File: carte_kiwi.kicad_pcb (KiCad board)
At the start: 2 copper layers, 50 x 50 mm, 236 parts, among them IC1 MCP2562, P1 CONN_01X05, P2 CONN_01X03, P3 CONN_01X05, P4 CONN_01X03, P5 Serial Wire, P6 CAN_conn, P7 CONN_01X03, P8 CONN_01X03, P9 CAN_conn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

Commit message: ajout nom, url et export gerber
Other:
- board text added: "Phoenix Robotik Carte Kiwi"
- board text added: "https://github.com/PhoenixRobotik/kiwi-elec"
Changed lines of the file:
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@@
     (area 124.924999 84.924999 175.075001 135.075001)
     (thickness 1.6)
-    (drawings 18)
+    (drawings 20)
     (tracks 463)
     (zones 0)
@@
   (page A4)
   (layers
-    (0 F.Cu signal)
-    (31 B.Cu signal)
-    (32 B.Adhes user)
-    (33 F.Adhes user)
-    (34 B.Paste user)
-    (35 F.Paste user)
+    (0 F.Cu signal hide)
+    (31 B.Cu signal hide)
+    (32 B.Adhes user hide)
+    (33 F.Adhes user hide)
+    (34 B.Paste user hide)
+    (35 F.Paste user hide)
     (36 B.SilkS user)
     (37 F.SilkS user)
     (38 B.Mask user hide)
     (39 F.Mask user hide)
-    (40 Dwgs.User user)
-    (41 Cmts.User user)
-    (42 Eco1.User user)
-    (43 Eco2.User user)
+    (40 Dwgs.User user hide)
+    (41 Cmts.User user hide)
+    (42 Eco1.User user hide)
+    (43 Eco2.User user hide)
     (44 Edge.Cuts user)
-    (45 Margin user)
+    (45 Margin user hide)
     (46 B.CrtYd user)
     (47 F.CrtYd user)
@@
     (visible_elements FFFFFF7F)
     (pcbplotparams
-      (layerselection 0x00030_80000001)
+      (layerselection 0x0c0fc_80000001)
       (usegerberextensions false)
       (excludeedgelayer true)
@@
       (outputformat 1)
       (mirror false)
-      (drillshape 1)
+      (drillshape 0)
       (scaleselection 1)
-      (outputdirectory ""))
+      (outputdirectory gerber/))
   )
   (net 0 "")
@@
       (net 36 "Net-(U3-Pad9)"))
   )
+  (gr_text https://github.com/PhoenixRobotik/kiwi-elec (at 143 133.5) (layer B.SilkS)
+    (effects (font (size 0.7 0.7) (thickness 0.175)) (justify mirror))
+  )
+  (gr_text "Phoenix Robotik\nCarte Kiwi" (at 141.75 130.75) (layer F.SilkS)
+    (effects (font (size 1.5 1.5) (thickness 0.3)))
+  )
   (gr_text PWR (at 133.26 125.78) (layer F.SilkS)

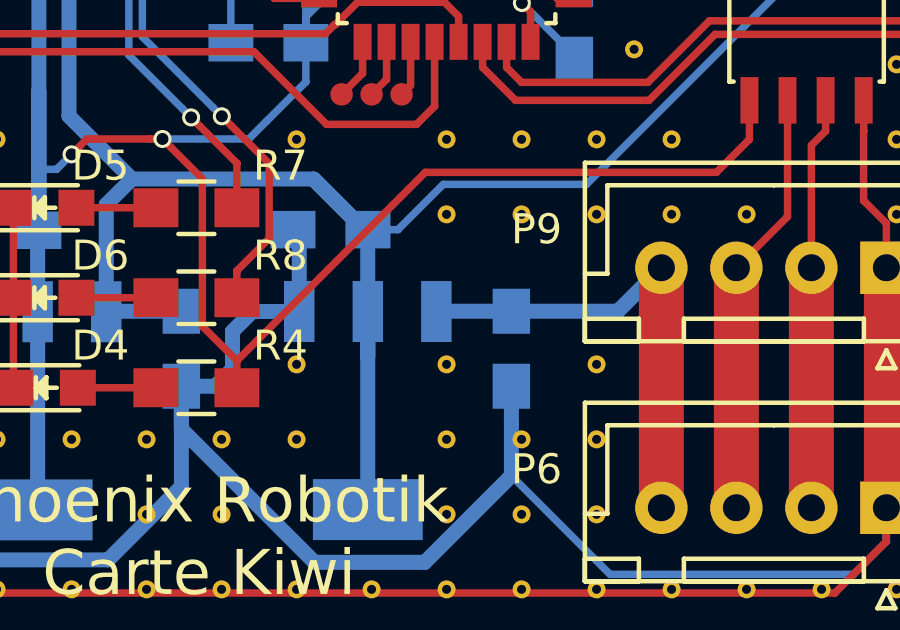
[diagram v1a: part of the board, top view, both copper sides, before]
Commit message: added OpenHW logo
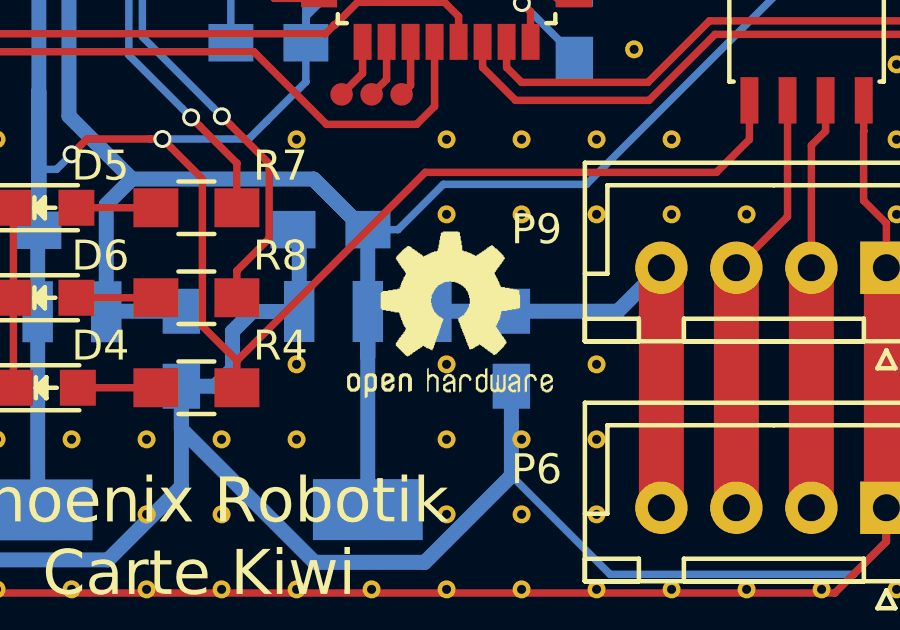
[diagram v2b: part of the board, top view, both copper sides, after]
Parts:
- added G***: LOGO, OPENHARDWARE:OSHWLOGO0.3IN, F.Cu at (146.3, 119.6)

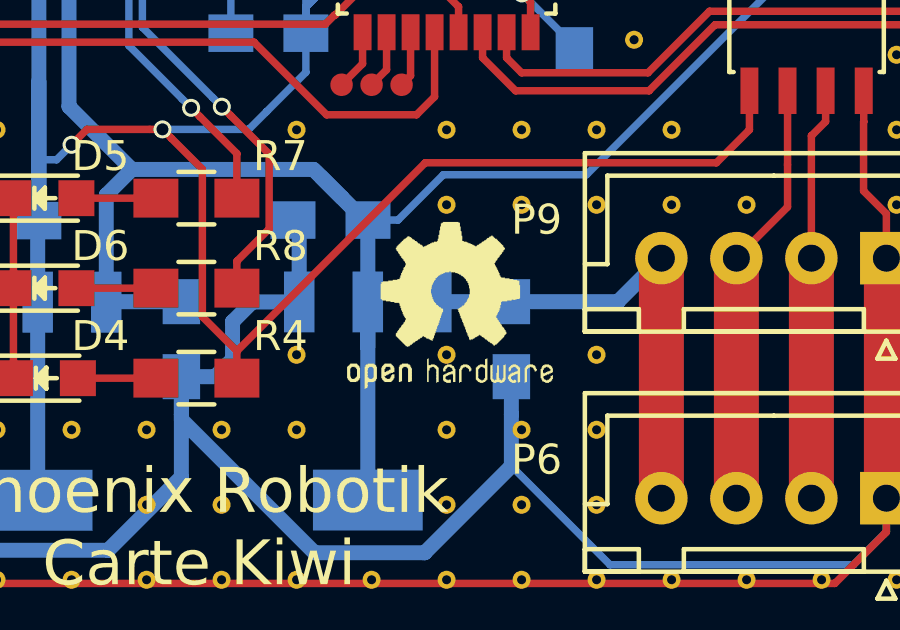
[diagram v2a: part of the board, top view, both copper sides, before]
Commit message: correct OSHW logo
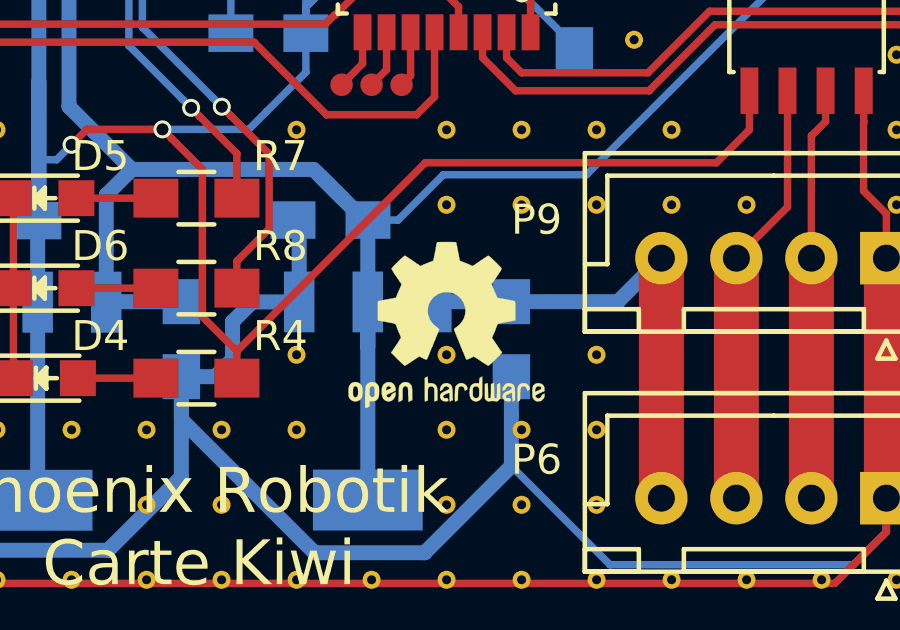
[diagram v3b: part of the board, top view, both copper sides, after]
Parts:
- removed G***: LOGO, OPENHARDWARE:OSHWLOGO0.3IN
- added REF***: OSHW-Logo2_7.3x6mm_SilkScreen, Symbols:OSHW-Logo2_7.3x6mm_SilkScreen, F.Cu at (150.0, 124.0)

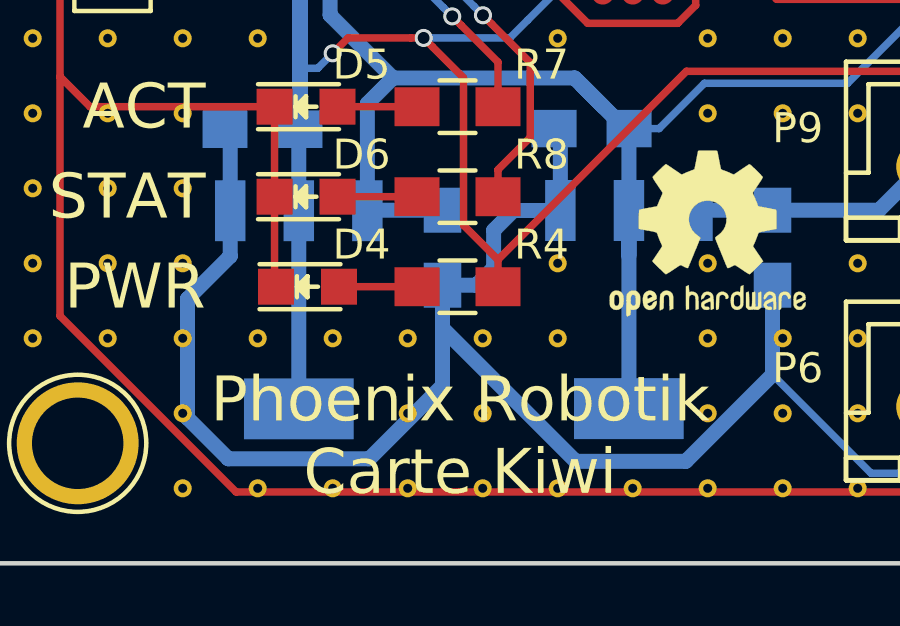
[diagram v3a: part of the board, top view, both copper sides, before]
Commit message: updated footprint
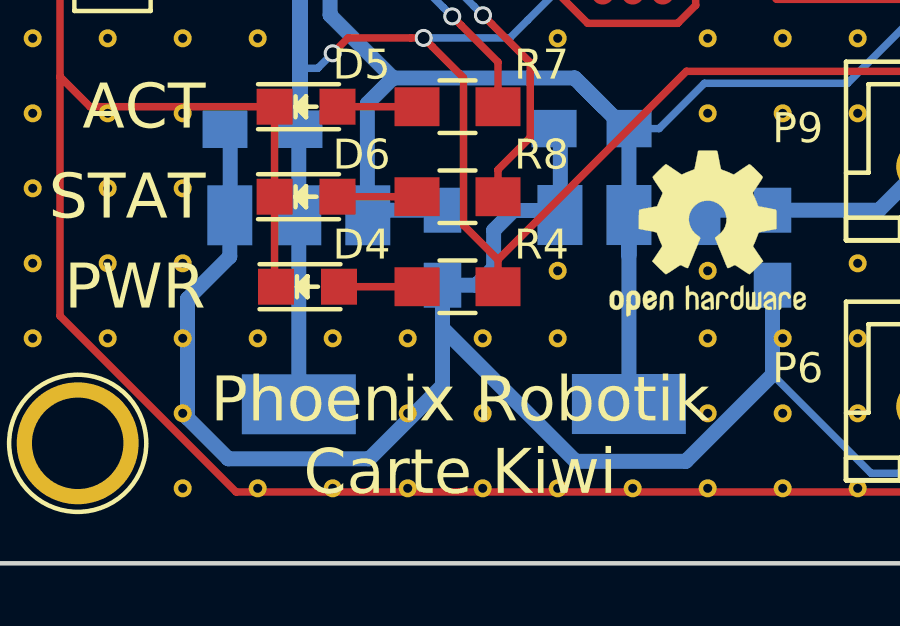
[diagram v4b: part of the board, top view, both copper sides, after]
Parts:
- U1, U2: footprint TO_SOT_Packages_SMD:SOT-223 -> TO_SOT_Packages_SMD:SOT-223-3Lead_TabPin2
- moved REF** 0.25 mm to (150.0, 125.2)
- moved REF** 0.25 mm to (145.0, 125.2)
- turned U1 to 270 degrees
- turned U2 to 270 degrees
